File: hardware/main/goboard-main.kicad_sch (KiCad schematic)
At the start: 12 parts, among them J1 USB_C_Receptacle_USB2.0, J2 Conn_02x05_Top_Bottom, J3 Conn_01x01, J4 Conn_01x03, SW11 SW_Push

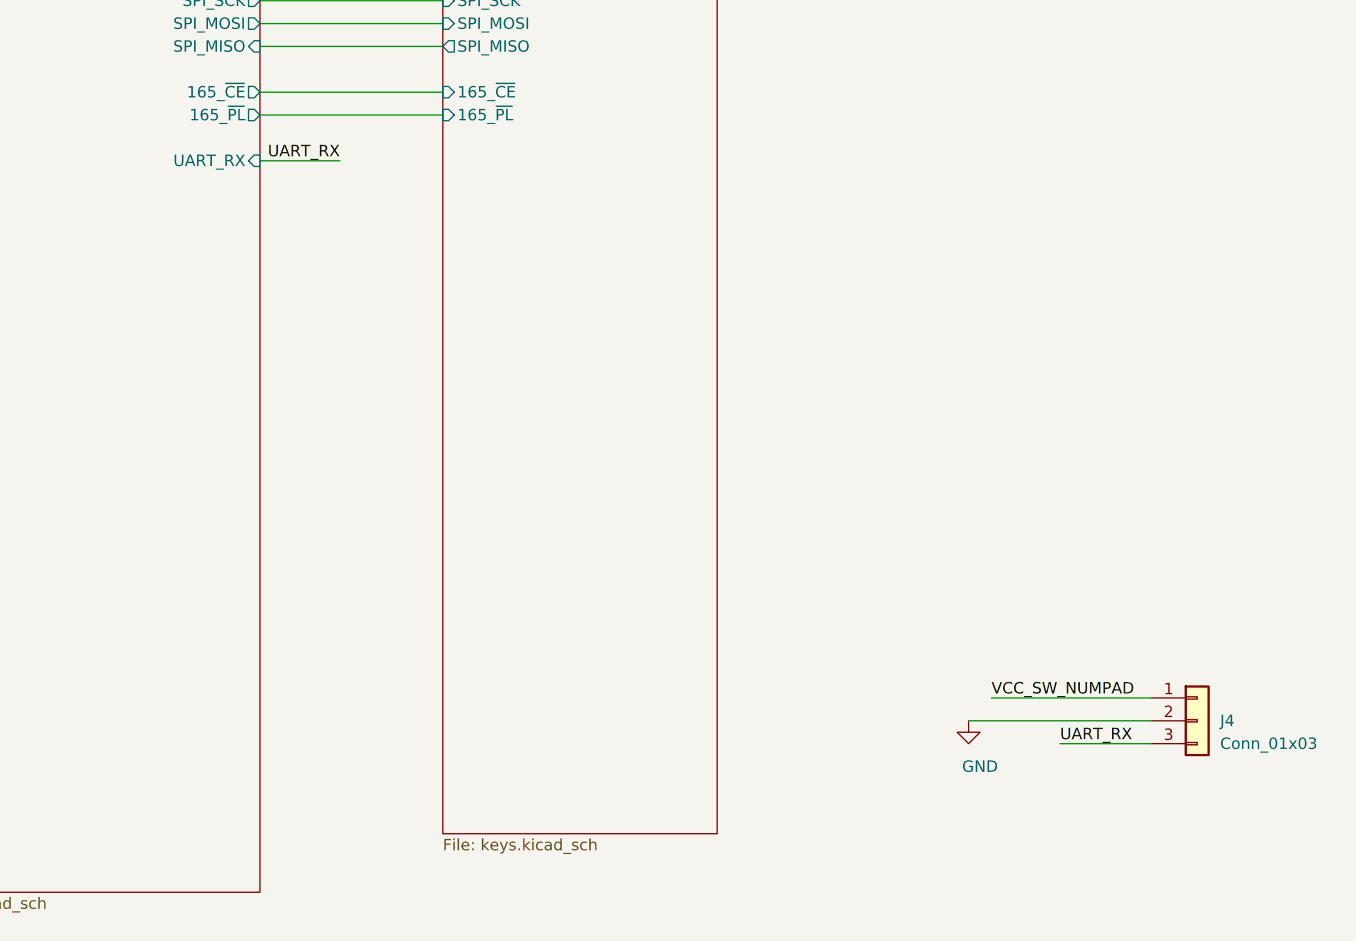
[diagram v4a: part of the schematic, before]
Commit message: Add a line for the UART direction main->numpad
This is necessary as the numlock-led is situated on the numpad and the
main mcu has to be able to switch it on and off.
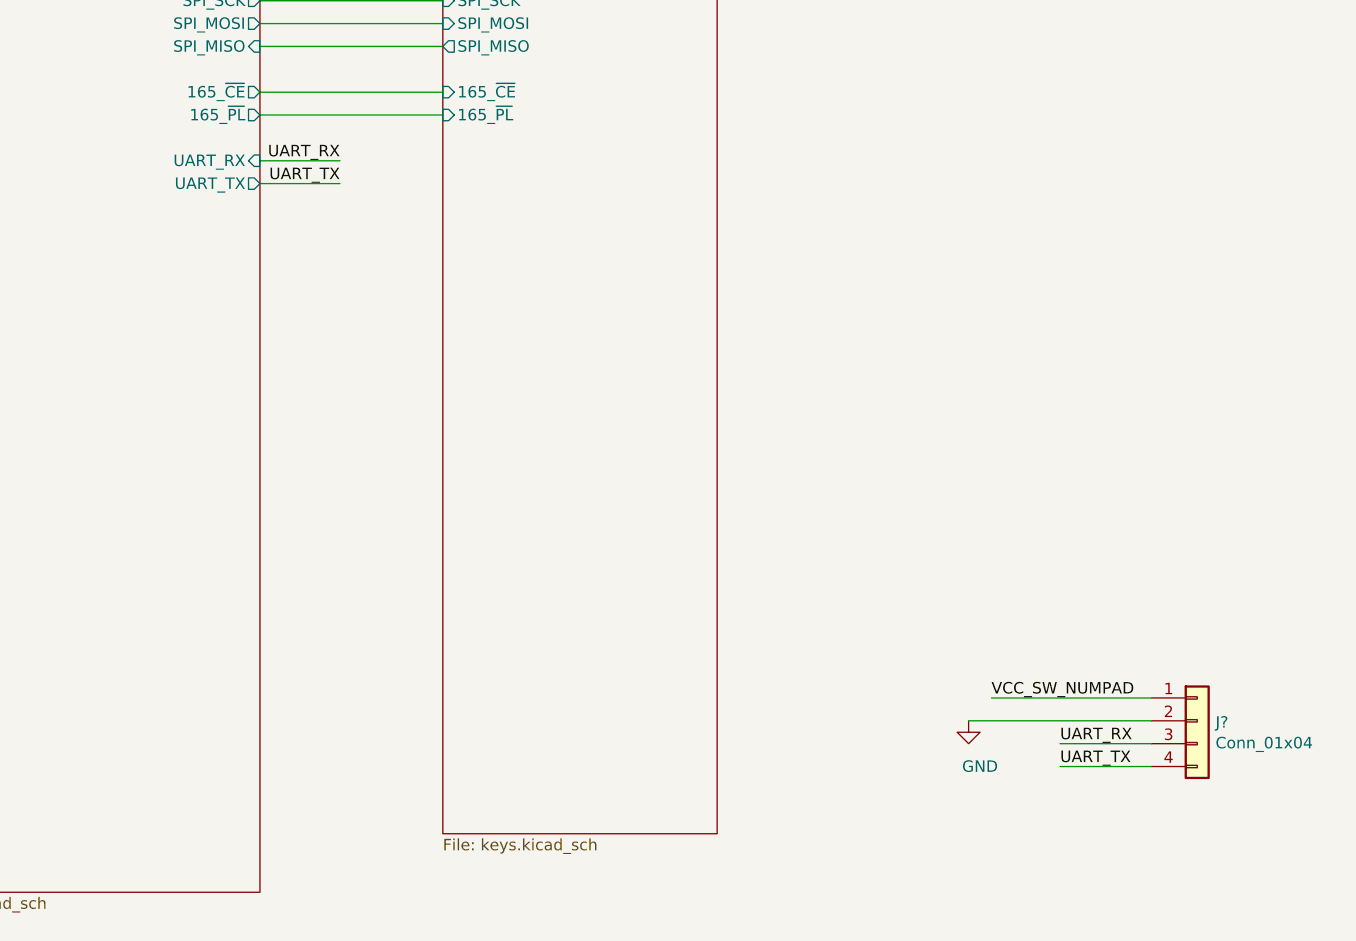
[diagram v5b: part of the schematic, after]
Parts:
- removed J4: Conn_01x03, symbol Connector_Generic:Conn_01x03
- added J?: Conn_01x04, symbol Connector_Generic:Conn_01x04
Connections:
- net GND: now also J?.2 (Pin_2)
- net UART_RX: now also J?.3 (Pin_3)
- net VCC_SW_NUMPAD: now also J?.1 (Pin_1)
- new net UART_TX: J?.4 (Pin_4)
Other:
- sheet MCU ports: added UART_TX; removed none
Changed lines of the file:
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@@
   (junction (at 80.01 91.44) (diameter 1.016) (color 0 0 0 0))
   (junction (at 86.36 60.96) (diameter 1.016) (color 0 0 0 0))
+  (no_connect (at 45.72 165.1))
+  (no_connect (at 41.91 63.5))
   (no_connect (at 33.02 170.18))
-  (no_connect (at 41.91 63.5))
   (no_connect (at 41.91 66.04))
   (no_connect (at 33.02 165.1))
-  (no_connect (at 45.72 165.1))
   (wire (pts (xy 19.05 73.66) (xy 19.05 76.2))
     (stroke (width 0) (type solid) (color 0 0 0 0))
@@
     (stroke (width 0) (type solid) (color 0 0 0 0))
   )
+  (wire (pts (xy 161.29 74.93) (xy 170.18 74.93))
+    (stroke (width 0) (type solid) (color 0 0 0 0))
+  )
   (wire (pts (xy 240.03 134.62) (xy 260.35 134.62))
     (stroke (width 0) (type solid) (color 0 0 0 0))
@@
   )
   (wire (pts (xy 250.19 137.16) (xy 260.35 137.16))
+    (stroke (width 0) (type solid) (color 0 0 0 0))
+  )
+  (wire (pts (xy 250.19 139.7) (xy 260.35 139.7))
     (stroke (width 0) (type solid) (color 0 0 0 0))
   )
@@
     (effects (font (size 1.27 1.27)) (justify right bottom))
   )
+  (label "UART_TX" (at 170.18 74.93 180)
+    (effects (font (size 1.27 1.27)) (justify right bottom))
+  )
   (label "VCC_SW_NUMPAD" (at 242.57 132.08 0)
     (effects (font (size 1.27 1.27)) (justify left bottom))
   )
   (label "UART_RX" (at 250.19 137.16 0)
+    (effects (font (size 1.27 1.27)) (justify left bottom))
+  )
+  (label "UART_TX" (at 250.19 139.7 0)
     (effects (font (size 1.27 1.27)) (justify left bottom))
   )
@@
     )
   )
-  (symbol (lib_id "Connector_Generic:Conn_01x03") (at 265.43 134.62 0) (unit 1)
-    (in_bom yes) (on_board yes)
-    (property "Reference" "J4" (id 0) (at 267.97 134.62 0)
-      (effects (font (size 1.27 1.27)) (justify left))
-    )
-    (property "Value" "Conn_01x03" (id 1) (at 267.97 137.16 0)
+  (symbol (lib_id "Connector_Generic:Conn_01x04") (at 265.43 134.62 0) (unit 1)
+    (in_bom yes) (on_board yes)
+    (property "Reference" "J?" (id 0) (at 267.4621 134.7914 0)
+      (effects (font (size 1.27 1.27)) (justify left))
+    )
+    (property "Value" "Conn_01x04" (id 1) (at 267.4621 137.0901 0)
       (effects (font (size 1.27 1.27)) (justify left))
     )
@@
       (effects (font (size 1.27 1.27)) (justify right))
     )
+    (pin "UART_TX" output (at 161.29 74.93 0)
+      (effects (font (size 1.27 1.27)) (justify right))
+    )
   )
   (sheet (at 27.94 106.68) (size 44.45 46.99)
@@
       (reference "J3") (unit 1) (value "Conn_01x01") (footprint "Connector_PinHeader_2.54mm:PinHeader_1x01_P2.54mm_Vertical")
     )
-    (path "/8f2168b0-9331-41f1-8b2a-0db0627517e9"
-      (reference "J4") (unit 1) (value "Conn_01x03") (footprint "")
+    (path "/9a9f26e6-288f-47d0-a7cc-10265fd1a76e"
+      (reference "J?") (unit 1) (value "Conn_01x04") (footprint "")
     )
     (path "/70bfc3f4-60ca-4487-a365-ec787e69545b"

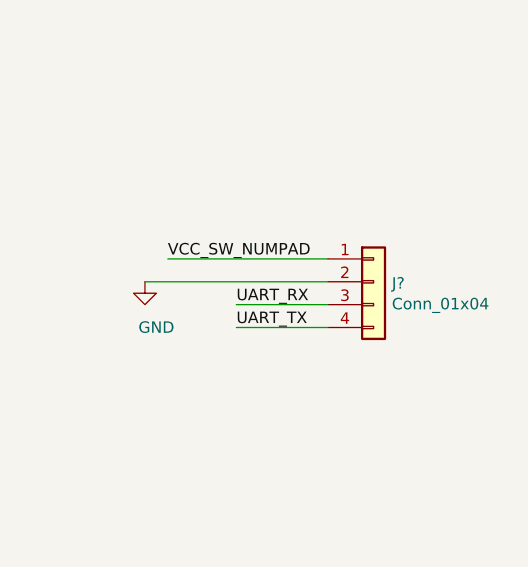
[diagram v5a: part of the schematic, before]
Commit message: Adapt the layout for another keycap set
The layout is now compatible with this keycap set:
https://hk-gaming.com/collections/keycaps/products/hk-gaming-dye-
sublimation-cherry-profile-thick-pbt-keysets-for-mechanical-keyboard-139
-keys-chalk
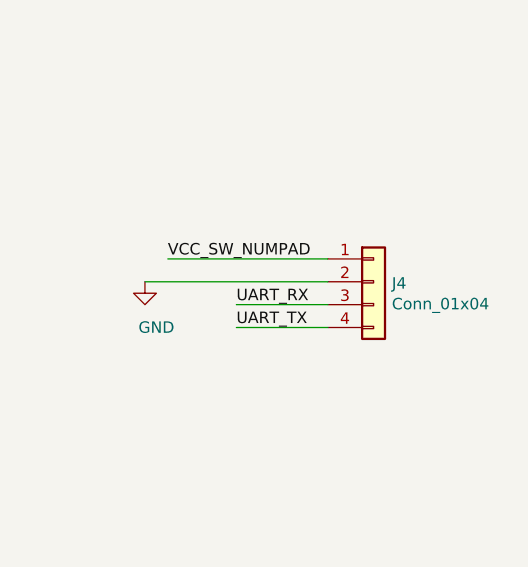
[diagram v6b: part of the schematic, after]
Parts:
- gave numbers to parts that had none: 1
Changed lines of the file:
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@@
   (junction (at 80.01 91.44) (diameter 1.016) (color 0 0 0 0))
   (junction (at 86.36 60.96) (diameter 1.016) (color 0 0 0 0))
+  (no_connect (at 41.91 66.04))
   (no_connect (at 45.72 165.1))
   (no_connect (at 41.91 63.5))
   (no_connect (at 33.02 170.18))
-  (no_connect (at 41.91 66.04))
   (no_connect (at 33.02 165.1))
   (wire (pts (xy 19.05 73.66) (xy 19.05 76.2))
@@
   (symbol (lib_id "Connector_Generic:Conn_01x04") (at 265.43 134.62 0) (unit 1)
     (in_bom yes) (on_board yes)
-    (property "Reference" "J?" (id 0) (at 267.4621 134.7914 0)
+    (property "Reference" "J4" (id 0) (at 267.4621 134.7914 0)
       (effects (font (size 1.27 1.27)) (justify left))
     )
@@
     )
     (path "/9a9f26e6-288f-47d0-a7cc-10265fd1a76e"
-      (reference "J?") (unit 1) (value "Conn_01x04") (footprint "")
+      (reference "J4") (unit 1) (value "Conn_01x04") (footprint "")
     )
     (path "/70bfc3f4-60ca-4487-a365-ec787e69545b"
@@
     )
     (path "/6ef23857-23de-44e2-ab0d-92ef0bfe30b4/b0f615c3-bc09-43de-bc7f-a05988c5ce22"
-      (reference "SW24") (unit 1) (value "Alt") (footprint "footprints:SW_Cherry_MX_1.00u_PCB")
+      (reference "SW24") (unit 1) (value "Alt") (footprint "footprints:SW_Cherry_MX_1.25u_PCB")
     )
     (path "/6ef23857-23de-44e2-ab0d-92ef0bfe30b4/570bd285-0cc2-40ea-be31-34fb8c419f66"
@@
     )
     (path "/6ef23857-23de-44e2-ab0d-92ef0bfe30b4/9a16c70a-0e33-4881-9e0c-218c8294cc90"
-      (reference "SW62") (unit 1) (value "Alt Gr") (footprint "footprints:SW_Cherry_MX_1.25u_PCB")
+      (reference "SW62") (unit 1) (value "Alt Gr") (footprint "footprints:SW_Cherry_MX_1.50u_PCB")
     )
     (path "/6ef23857-23de-44e2-ab0d-92ef0bfe30b4/373eb885-d3b9-43db-b344-563e7549b2c1"
@@
       (reference "SW66") (unit 1) (value "'") (footprint "footprints:SW_Cherry_MX_1.00u_PCB")
     )
-    (path "/6ef23857-23de-44e2-ab0d-92ef0bfe30b4/ac5acf19-6bc2-407a-8a8d-818f22c9bfcb"
-      (reference "SW67") (unit 1) (value "Menu") (footprint "footprints:SW_Cherry_MX_1.00u_PCB")
-    )
     (path "/6ef23857-23de-44e2-ab0d-92ef0bfe30b4/f82d6a6f-5230-4544-ac03-93b5a3044a51"
       (reference "SW68") (unit 1) (value "F12") (footprint "footprints:SW_Cherry_MX_1.00u_PCB")
@@
     )
     (path "/6ef23857-23de-44e2-ab0d-92ef0bfe30b4/33101199-2245-4847-8898-45a7e7746c03"
-      (reference "SW73") (unit 1) (value "Ctrl") (footprint "footprints:SW_Cherry_MX_1.00u_PCB")
+      (reference "SW73") (unit 1) (value "Ctrl") (footprint "footprints:SW_Cherry_MX_1.50u_PCB")
     )
     (path "/6ef23857-23de-44e2-ab0d-92ef0bfe30b4/ac8aea8d-3e23-4a20-a087-72c9265a740e"
